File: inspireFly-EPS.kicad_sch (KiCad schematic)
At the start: 182 parts, among them J1 USB4085-GF-A_REVB, J2 Conn_01x02_Pin, J3 FTSH-107-01-L-DV-K-A, Q1 SQJ123ELP-T1_GE3, Q10 SQJA62EP-T1_GE3, Q14 SQJA62EP-T1_GE3, Q15 SQJA62EP-T1_GE3, Q16 SQJA62EP-T1_GE3, Q17 SQJA62EP-T1_GE3, Q3 SQJA62EP-T1_GE3, Q4 SQJA62EP-T1_GE3, Q5 SQJA62EP-T1_GE3, Q6 SQJA62EP-T1_GE3, Q7 SQJA62EP-T1_GE3, Q8 SQJA62EP-T1_GE3, Q9 SQJA62EP-T1_GE3, SW1 SW_Push, SW2 SW_Push, SW3 SW_Push, U1 STM32U575RIT6, U10 BQ25756ERRVR, U13 TPS259472ARPWR, U2 BQ25750RRVR, U3 TCAN332DCNR, U4 MAX77504AAFC+T, U6 INA180A3IDBVT, U7 INA180A3IDBVT, U8 TPS63070RNMR, U9 TPS63070RNMR, Y1 Crystal_GND2

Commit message: Routing Updates
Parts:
- removed C1, C25: 100nF, Capacitor_SMD:C_0402_1005Metric_Pad0.74x0.62mm_HandSolder, symbol Device:C
- removed C26, C51: 10pF, Capacitor_SMD:C_0402_1005Metric_Pad0.74x0.62mm_HandSolder, symbol Device:C
- removed J1: USB4085-GF-A_REVB, inspireFly-EPS-footprints:GCT_USB4085-GF-A_REVB, symbol InspireFly-EPS-sym_lib:USB4085-GF-A_REVB
- removed R18, R19: 10k, Resistor_SMD:R_0402_1005Metric_Pad0.72x0.64mm_HandSolder, symbol Device:R_US
- removed R35, R36: 10K, Resistor_SMD:R_0402_1005Metric_Pad0.72x0.64mm_HandSolder, symbol Device:R_US
- removed SW1, SW2: SW_Push, inspireFly-EPS-footprints:SW_PTS810_SJM_250_SMTR_LFS, symbol Switch:SW_Push
- removed U1: STM32U575RIT6, inspireFly-EPS-footprints:LQFP64-10x10mm_STM, symbol InspireFly-EPS-sym_lib:STM32U575RIT6
- removed Y1: Crystal_GND2, inspireFly-EPS-footprints:XTAL_TSX-3225_16.0000MF18X-AC0, symbol Device:Crystal_GND2
- added C25, C26: 22pF, Capacitor_SMD:C_0402_1005Metric_Pad0.74x0.62mm_HandSolder, symbol Device:C_Small
- added J5: USB4110-GF-A, inspireFly-EPS-footprints:USB4110-GF-A_GCT, symbol inspirefly:USB4110-GF-A
- added R54: 100k, Resistor_SMD:R_0402_1005Metric_Pad0.72x0.64mm_HandSolder, symbol Device:R_US
- added RN1: YC158TJR-072K2L, inspireFly-EPS-footprints:RESCAXE64P320X160X70-10N, symbol inspirefly:YC158TJR-072K2L
- added SW4: SW_TL1015AF160QG, inspireFly-EPS-footprints:SW_TL1015AF160QG, symbol Switch:SW_Push
- added U5: STM32U575CIT6, inspireFly-EPS-footprints:LQFP48-7x7mm_STM, symbol InspireFly-EPS-sym_lib:STM32U575CIT6
- added Y2: XTAL_ABS07-32.768KHZ-T, inspireFly-EPS-footprints:XTAL_ABS07-32.768KHZ-T, symbol Device:Crystal
- C10, C11, C12, C13, C15, C16, C17, C18, C19, C20, C21, C22, C23, C35, C36, C50, D4, D5, L1, Q1, Q10, Q3, Q4, Q5, Q6, Q7, Q8, Q9, R1, R12, R13, R14, R15, R2, R3, R33, R34, R4, R5, R6, R7, R8, R9, TP1, TP2, TP5, U2: now left out of the parts list
- C6: value 10uF -> 1uF
- D1, R20, R21: now not fitted; now left out of the parts list
- JP2: footprint inspirefly:SmallJumper -> Jumper:SolderJumper-2_P1.3mm_Open_TrianglePad1.0x1.5mm
- R37: value 10K -> 10k
- SW3: value SW_Push -> SW_TL1015AF160QG; footprint inspireFly-EPS-footprints:SW_PTS810_SJM_250_SMTR_LFS -> inspireFly-EPS-footprints:SW_TL1015AF160QG
- U10: footprint inspirefly:IC_BQ25756ERRVR -> inspireFly-EPS-footprints:IC_BQ25756ERRVR
- U13: footprint inspirefly:RPW0010A-MFG -> inspireFly-EPS-footprints:RPW0010A-MFG
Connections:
- net +3.3V: now also R37.1, RN1.10, RN1.5, SW4.2, U5.1 (VBAT), U5.24 (VDD), U5.36 (VDD), U5.48 (VDD), U5.9 (VDDA); no longer R37.2
- net ADC1_IN3: now also U5.10 (PA0)
- net ADC1_IN4: now also U5.11 (PA1)
- net EXTERNAL_VOLTAGE: now also D2.1 (K), J2.1 (Pin_1), TP6.1
- net GND: now also C79.2, SW3.2, C25.1, C26.1, J5.15 (Shield), J5.16 (Shield), J5.17 (Shield), J5.18 (Shield), J5.A1-B12 (GND), J5.A12-B1 (GND), R54.1, U5.23 (VSS), U5.35 (VSS), U5.47 (VSS), U5.8 (VSSA); no longer SW3.1
- net I2C2_SCL: now also RN1.4, U5.26 (PB13)
- net I2C2_SDA: now also RN1.3, U5.27 (PB14)
- net JTCK/SWCLK: now also U5.37 (PA14)
- net JTDI: now also U5.38 (PA15)
- net JTMS/SWDIO: now also U5.34 (PA13)
- net NRST: now also R37.2, SW3.1, U5.7 (NRST); no longer R37.1, SW3.2
- net PROTECTED_VOLTAGE: now also C30.1, C37.1, C44.1, U4.12 (SUP), U4.2 (EN), U8.1 (PS/SYNC), U8.12_13 (VIN), U8.14 (EN), U9.1 (PS/SYNC), U9.12_13 (VIN), U9.14 (EN)
- net SWO: now also U5.39 (PB3)
- net USB_CC1: now also J5.A5 (CC1), U5.41 (PB5)
- net USB_CC2: now also J5.B5 (CC2), U5.28 (PB15)
- net USB_V: now also J5.A4-B9 (VBUS), J5.A9-B4 (VBUS)
- net V_BUS_COMBINED: no longer D2.1 (K), J2.1 (Pin_1), TP6.1
- net V_PROTECTED: no longer C30.1, C37.1, C44.1, U4.12 (SUP), U4.2 (EN), U8.1 (PS/SYNC), U8.12_13 (VIN), U8.14 (EN), U9.1 (PS/SYNC), U9.12_13 (VIN), U9.14 (EN)
- net DEBUG_LPUART_TX: now reaches J3.13
- net DEBUG_LPUART_TX: now also U5.12 (PA2)
- net DEBUG_LPUART_RX: now reaches J3.14
- net DEBUG_LPUART_RX: now also U5.13 (PA3)
- net at C2.1: now also U5.22 (VCAP)
- new net: C25.2, U5.3 (PC14-OSC32_IN), Y2.1
- new net: C26.2, U5.4 (PC15-OSC32_OUT), Y2.2
- new net BOOT0: R54.2, SW4.1, U5.44 (PH3-BOOT0)
- new net CAN_RXD: U5.32 (PA11)
- new net CAN_TXD: U5.33 (PA12)
- new net I2C1_SCL: RN1.2, U5.45 (PB8)
- new net I2C1_SDA: RN1.1, U5.46 (PB9)
- new net I2C3_SCL: RN1.8, U5.17 (PA7)
- new net I2C3_SDA: RN1.9, U5.40 (PB4)
- new net I2C4_SCL: RN1.6, U5.21 (PB10)
- new net I2C4_SDA: RN1.7, U5.43 (PB7)
- no-connect marks 19 -> 21
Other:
- note removed: "NRST Circuit"

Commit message: Schematic Updates
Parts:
- added C80: 22uF, Capacitor_SMD:C_0805_2012Metric_Pad1.18x1.45mm_HandSolder, symbol Device:C
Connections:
- net EXTERNAL_VOLTAGE: now also C80.1
- net GND: now also C80.2
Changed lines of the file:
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@@
 	)
 	(junction
+		(at 261.62 193.04)
+		(diameter 0)
+		(color 0 0 0 0)
+	)
+	(junction
 		(at 265.43 566.42)
 		(diameter 0)
@@
 	)
 	(symbol
+		(lib_id "Device:C")
+		(at 261.62 189.23 180)
+		(unit 1)
+		(body_style 1)
+		(exclude_from_sim no)
+		(in_bom yes)
+		(on_board yes)
+		(in_pos_files yes)
+		(dnp no)
+		(fields_autoplaced yes)
+		(property "Reference" "C80"
+			(at 257.81 190.5001 0)
+			(show_name no)
+			(do_not_autoplace no)
+			(effects
+				(font
+					(size 1.27 1.27)
+				)
+				(justify left)
+			)
+		)
+		(property "Value" "22uF"
+			(at 257.81 187.9601 0)
+			(show_name no)
+			(do_not_autoplace no)
+			(effects
+				(font
+					(size 1.27 1.27)
+				)
+				(justify left)
+			)
+		)
+		(property "Footprint" "Capacitor_SMD:C_0805_2012Metric_Pad1.18x1.45mm_HandSolder"
+			(at 260.6548 185.42 0)
+			(hide yes)
+			(show_name no)
+			(do_not_autoplace no)
+			(effects
+				(font
+					(size 1.27 1.27)
+				)
+			)
+		)
+		(property "Datasheet" ""
+			(at 261.62 189.23 0)
+			(hide yes)
+			(show_name no)
+			(do_not_autoplace no)
+			(effects
+				(font
+					(size 1.27 1.27)
+				)
+			)
+		)
+		(property "Description" "Unpolarized capacitor"
+			(at 261.62 189.23 0)
+			(hide yes)
+			(show_name no)
+			(do_not_autoplace no)
+			(effects
+				(font
+					(size 1.27 1.27)
+				)
+			)
+		)
+		(pin "2"
+		)
+		(pin "1"
+		)
+		(instances
+			(project "inspireFly-EPS"
+				(path "/85d7bd69-2813-405d-9eae-82e9bb551a95"
+					(reference "C80")
+					(unit 1)
+				)
+			)
+		)
+	)
+	(symbol
 		(lib_id "power:+3.3V")
 		(at 231.14 83.82 0)
@@
 					(unit 1)
 				)
+			)
+		)
+	)
+	(symbol
+		(lib_id "power:GND")
+		(at 261.62 185.42 180)
+		(unit 1)
+		(body_style 1)
+		(exclude_from_sim no)
+		(in_bom yes)
+		(on_board yes)
+		(in_pos_files yes)
+		(dnp no)
+		(property "Reference" "#PWR0125"
+			(at 261.62 179.07 0)
+			(hide yes)
+			(show_name no)
+			(do_not_autoplace no)
+			(effects
+				(font
+					(size 1.27 1.27)
+				)
+			)
+		)
+		(property "Value" "GND"
+			(at 261.366 181.61 0)
+			(show_name no)
+			(do_not_autoplace no)
+			(effects
+				(font
+					(size 1.27 1.27)
+				)
+			)
+		)
+		(property "Footprint" ""
+			(at 261.62 185.42 0)
+			(hide yes)
+			(show_name no)
+			(do_not_autoplace no)
+			(effects
+				(font
+					(size 1.27 1.27)
+				)
+			)
+		)
+		(property "Datasheet" ""
+			(at 261.62 185.42 0)
+			(hide yes)
+			(show_name no)
+			(do_not_autoplace no)
+			(effects
+				(font
+					(size 1.27 1.27)
+				)
+			)
+		)
+		(property "Description" "Power symbol creates a global label with name \"GND\" , ground"
+			(at 261.62 185.42 0)
+			(hide yes)
+			(show_name no)
+			(do_not_autoplace no)
+			(effects
+				(font
+					(size 1.27 1.27)
+				)
+			)
+		)
+		(pin "1"
+		)
+		(instances
+			(project "inspireFly-EPS"
+				(path "/85d7bd69-2813-405d-9eae-82e9bb551a95"
+					(reference "#PWR0125")
+					(unit 1)
+				)

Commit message: 3.3V routing changes
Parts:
- removed C34, C41: 22uF, Capacitor_SMD:C_0805_2012Metric_Pad1.18x1.45mm_HandSolder, symbol Device:C
- added J4: Conn_01x02_Pin, Connector_PinSocket_2.54mm:PinSocket_1x02_P2.54mm_Vertical, symbol Connector:Conn_01x02_Pin
- C30, C37, C38, C44, C45: footprint Capacitor_SMD:C_0805_2012Metric_Pad1.18x1.45mm_HandSolder -> Capacitor_SMD:C_0402_1005Metric_Pad0.74x0.62mm_HandSolder
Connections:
- net CAN_H: now also J4.1 (Pin_1)
- net CAN_L: now also J4.2 (Pin_2)
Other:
- moved on the sheet: C31, C42, C43

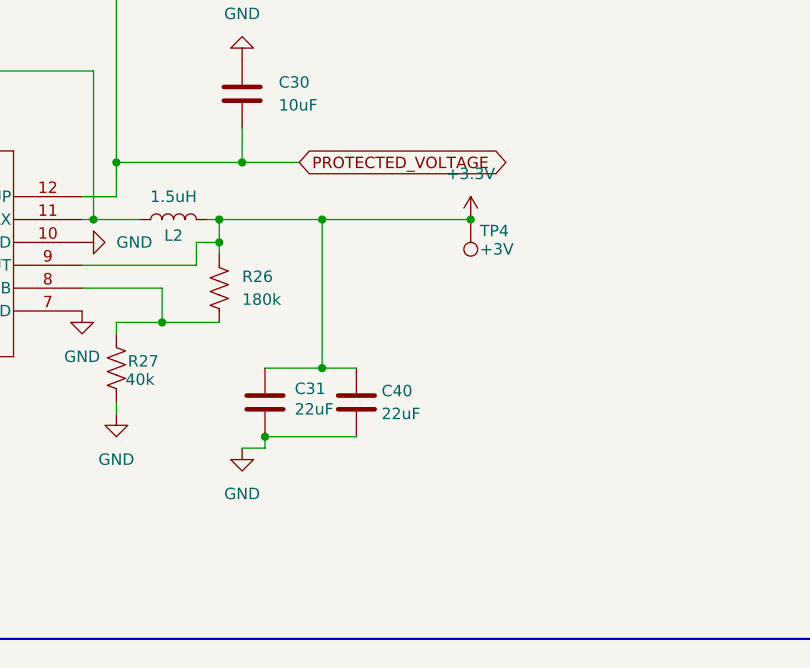
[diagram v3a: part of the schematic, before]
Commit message: Pushing routing changes, finailize vreg locations
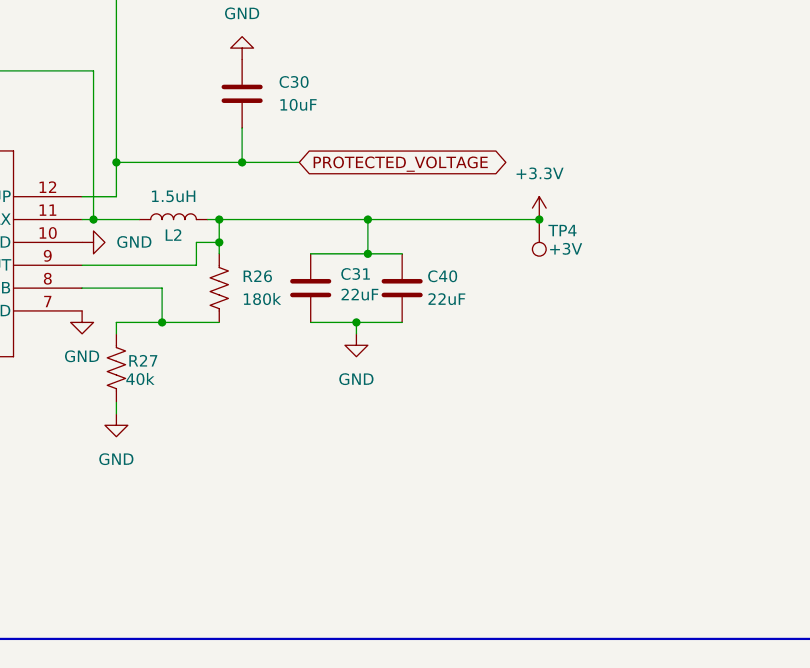
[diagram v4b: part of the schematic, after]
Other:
- moved on the sheet: C31, C40, TP4
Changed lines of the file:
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@@
 	)
 	(junction
-		(at 102.87 588.01)
+		(at 429.26 213.36)
 		(diameter 0)
 		(color 0 0 0 0)
 	)
 	(junction
-		(at 194.31 86.36)
+		(at 102.87 588.01)
 		(diameter 0)
 		(color 0 0 0 0)
 	)
 	(junction
-		(at 134.62 566.42)
+		(at 194.31 86.36)
 		(diameter 0)
 		(color 0 0 0 0)
 	)
 	(junction
-		(at 218.44 566.42)
+		(at 134.62 566.42)
 		(diameter 0)
 		(color 0 0 0 0)
 	)
 	(junction
-		(at 421.64 213.36)
+		(at 218.44 566.42)
 		(diameter 0)
 		(color 0 0 0 0)
@@
 	)
 	(junction
-		(at 405.13 213.36)
+		(at 410.21 213.36)
+		(diameter 0)
+		(color 0 0 0 0)
+	)
+	(junction
+		(at 408.94 224.79)
 		(diameter 0)
 		(color 0 0 0 0)
@@
 	)
 	(junction
-		(at 398.78 237.49)
-		(diameter 0)
-		(color 0 0 0 0)
-	)
-	(junction
 		(at 187.96 222.25)
 		(diameter 0)
@@
 	)
 	(junction
-		(at 405.13 229.87)
+		(at 410.21 217.17)
 		(diameter 0)
 		(color 0 0 0 0)
@@
 	(wire
 		(pts
-			(xy 398.78 238.76) (xy 396.24 238.76)
+			(xy 408.94 224.79) (xy 408.94 226.06)
 		)
 		(stroke
@@
 	(wire
 		(pts
-			(xy 398.78 237.49) (xy 408.94 237.49)
+			(xy 403.86 224.79) (xy 408.94 224.79)
 		)
 		(stroke
@@
 	(wire
 		(pts
-			(xy 405.13 213.36) (xy 405.13 229.87)
+			(xy 410.21 213.36) (xy 410.21 217.17)
 		)
 		(stroke
@@
 	(wire
 		(pts
-			(xy 398.78 238.76) (xy 398.78 237.49)
+			(xy 295.91 370.84) (xy 295.91 372.11)
 		)
 		(stroke
@@
 	(wire
 		(pts
-			(xy 295.91 370.84) (xy 295.91 372.11)
+			(xy 477.52 284.48) (xy 477.52 281.94)
 		)
 		(stroke
@@
 	(wire
 		(pts
-			(xy 477.52 284.48) (xy 477.52 281.94)
+			(xy 74.93 368.3) (xy 74.93 359.41)
 		)
 		(stroke
@@
 	(wire
 		(pts
-			(xy 74.93 368.3) (xy 74.93 359.41)
+			(xy 105.41 494.03) (xy 128.27 494.03)
 		)
 		(stroke
@@
 	(wire
 		(pts
-			(xy 105.41 494.03) (xy 128.27 494.03)
+			(xy 321.31 226.06) (xy 321.31 220.98)
 		)
 		(stroke
@@
 	(wire
 		(pts
-			(xy 321.31 226.06) (xy 321.31 220.98)
+			(xy 337.82 60.96) (xy 355.6 60.96)
 		)
 		(stroke
@@
 	(wire
 		(pts
-			(xy 337.82 60.96) (xy 355.6 60.96)
+			(xy 408.94 224.79) (xy 414.02 224.79)
 		)
 		(stroke
@@
 	(wire
 		(pts
-			(xy 393.7 213.36) (xy 405.13 213.36)
+			(xy 393.7 213.36) (xy 410.21 213.36)
 		)
 		(stroke
@@
 	(wire
 		(pts
-			(xy 405.13 213.36) (xy 421.64 213.36)
-		)
-		(stroke
-			(width 0)
-			(type default)
-		)
-	)
-	(wire
-		(pts
 			(xy 220.98 382.27) (xy 306.07 382.27)
 		)
@@
 	(wire
 		(pts
+			(xy 410.21 213.36) (xy 429.26 213.36)
+		)
+		(stroke
+			(width 0)
+			(type default)
+		)
+	)
+	(wire
+		(pts
 			(xy 260.35 342.9) (xy 271.78 342.9)
 		)
@@
 	(wire
 		(pts
-			(xy 398.78 229.87) (xy 405.13 229.87)
+			(xy 403.86 217.17) (xy 410.21 217.17)
 		)
 		(stroke
@@
 	(wire
 		(pts
-			(xy 405.13 229.87) (xy 408.94 229.87)
+			(xy 410.21 217.17) (xy 414.02 217.17)
 		)
 		(stroke
@@
 	(symbol
 		(lib_id "power:+3.3V")
-		(at 421.64 213.36 0)
+		(at 429.26 213.36 0)
 		(unit 1)
 		(body_style 1)
@@
 		(fields_autoplaced yes)
 		(property "Reference" "#PWR037"
-			(at 421.64 217.17 0)
+			(at 429.26 217.17 0)
 			(hide yes)
 			(show_name no)
@@
 		)
 		(property "Value" "+3.3V"
-			(at 421.64 208.28 0)
+			(at 429.26 208.28 0)
 			(show_name no)
 			(do_not_autoplace no)
@@
 		)
 		(property "Footprint" ""
-			(at 421.64 213.36 0)
+			(at 429.26 213.36 0)
 			(hide yes)
 			(show_name no)
@@
 		)
 		(property "Datasheet" ""
-			(at 421.64 213.36 0)
+			(at 429.26 213.36 0)
 			(hide yes)
 			(show_name no)
@@
 		)
 		(property "Description" "Power symbol creates a global label with name \"+3.3V\""
-			(at 421.64 213.36 0)
+			(at 429.26 213.36 0)
 			(hide yes)
 			(show_name no)
@@
 	(symbol
 		(lib_id "Device:C")
-		(at 408.94 233.68 180)
+		(at 414.02 220.98 180)
 		(unit 1)
 		(body_style 1)
@@
 		(dnp no)
 		(property "Reference" "C40"
-			(at 411.734 232.41 0)
+			(at 416.814 219.71 0)
 			(show_name no)
 			(do_not_autoplace no)
@@
 		)
 		(property "Value" "22uF"
-			(at 411.734 234.95 0)
+			(at 416.814 222.25 0)
 			(show_name no)
 			(do_not_autoplace no)
@@
 		)
 		(property "Footprint" "Capacitor_SMD:C_0805_2012Metric_Pad1.18x1.45mm_HandSolder"
-			(at 407.9748 229.87 0)
+			(at 413.0548 217.17 0)
 			(hide yes)
 			(show_name no)
@@
 		)
 		(property "Datasheet" ""
-			(at 408.94 233.68 0)
+			(at 414.02 220.98 0)
 			(hide yes)
 			(show_name no)
@@
 		)
 		(property "Description" "Unpolarized capacitor"
-			(at 408.94 233.68 0)
+			(at 414.02 220.98 0)
 			(hide yes)
 			(show_name no)
@@
 	(symbol
 		(lib_id "Connector:TestPoint")
-		(at 421.64 213.36 180)
+		(at 429.26 213.36 180)
 		(unit 1)
 		(body_style 1)
@@
 		(dnp no)
 		(property "Reference" "TP4"
-			(at 422.656 214.63 0)
+			(at 430.276 214.63 0)
 			(show_name no)
 			(do_not_autoplace no)
@@
 		)
 		(property "Value" "+3V"
-			(at 422.656 216.662 0)
+			(at 430.276 216.662 0)
 			(show_name no)
 			(do_not_autoplace no)
@@
 		)
 		(property "Footprint" "TestPoint:TestPoint_Pad_D1.5mm"
-			(at 416.56 213.36 0)
+			(at 424.18 213.36 0)
 			(hide yes)
 			(show_name no)
@@
 		)
 		(property "Datasheet" ""
-			(at 416.56 213.36 0)
+			(at 424.18 213.36 0)
 			(hide yes)
 			(show_name no)
@@
 		)
 		(property "Description" "test point"
-			(at 421.64 213.36 0)
+			(at 429.26 213.36 0)
 			(hide yes)
 			(show_name no)
@@
 	(symbol
 		(lib_id "Device:C")
-		(at 398.78 233.68 180)
+		(at 403.86 220.98 180)
 		(unit 1)
 		(body_style 1)
@@
 		(dnp no)
 		(property "Reference" "C31"
-			(at 402.082 232.156 0)
+			(at 407.162 219.456 0)
 			(show_name no)
 			(do_not_autoplace no)
@@
 		)
 		(property "Value" "22uF"
-			(at 402.082 234.442 0)
+			(at 407.162 221.742 0)
 			(show_name no)
 			(do_not_autoplace no)
@@
 		)
 		(property "Footprint" "Capacitor_SMD:C_0805_2012Metric_Pad1.18x1.45mm_HandSolder"
-			(at 397.8148 229.87 0)
+			(at 402.8948 217.17 0)
 			(hide yes)
 			(show_name no)
@@
 		)
 		(property "Datasheet" ""
-			(at 398.78 233.68 0)
+			(at 403.86 220.98 0)
 			(hide yes)
 			(show_name no)
@@
 		)
 		(property "Description" "Unpolarized capacitor"
-			(at 398.78 233.68 0)
+			(at 403.86 220.98 0)
 			(hide yes)
 			(show_name no)
@@
 	(symbol
 		(lib_id "power:GND")
-		(at 396.24 238.76 0)
+		(at 408.94 226.06 0)
 		(unit 1)
 		(body_style 1)
@@
 		(fields_autoplaced yes)
 		(property "Reference" "#PWR047"
-			(at 396.24 245.11 0)
+			(at 408.94 232.41 0)
 			(hide yes)
 			(show_name no)
@@
 		)
 		(property "Value" "GND"
-			(at 396.24 243.84 0)
+			(at 408.94 231.14 0)
 			(show_name no)
 			(do_not_autoplace no)
@@
 		)
 		(property "Footprint" ""
-			(at 396.24 238.76 0)
+			(at 408.94 226.06 0)
 			(hide yes)
 			(show_name no)
@@
 		)
 		(property "Datasheet" ""
-			(at 396.24 238.76 0)
+			(at 408.94 226.06 0)
 			(hide yes)
 			(show_name no)
@@
 		)
 		(property "Description" "Power symbol creates a global label with name \"GND\" , ground"
-			(at 396.24 238.76 0)
+			(at 408.94 226.06 0)
 			(hide yes)
 			(show_name no)

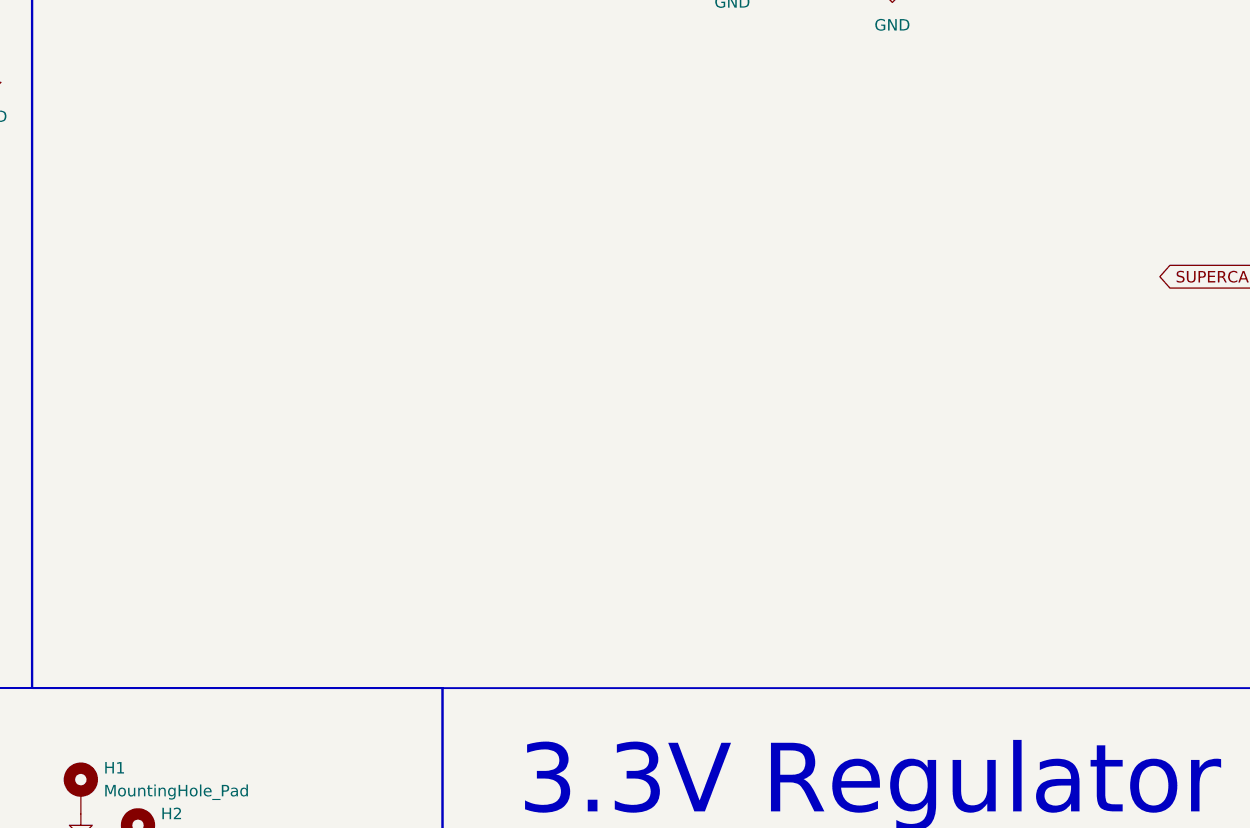
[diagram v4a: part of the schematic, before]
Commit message: Added linear charger to schematic
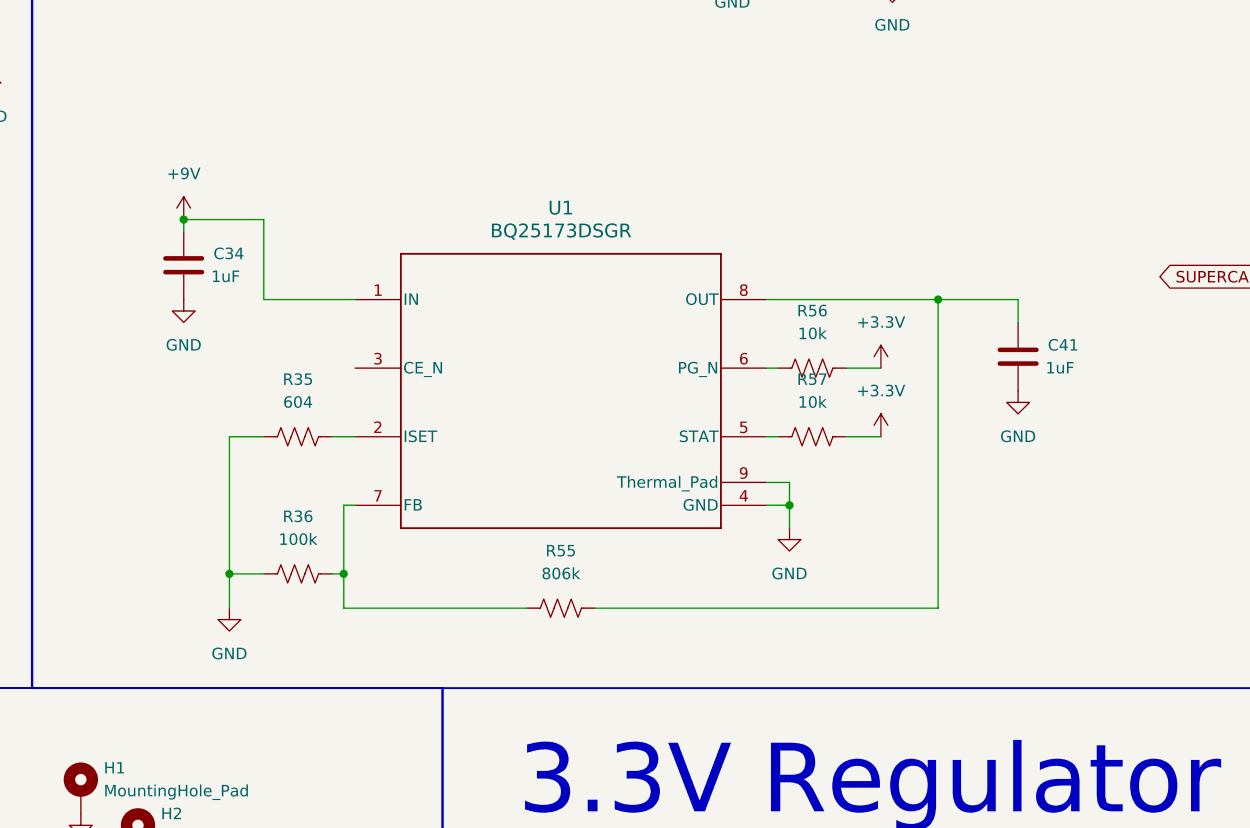
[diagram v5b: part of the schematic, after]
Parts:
- added C34, C41: 1uF, Capacitor_SMD:C_0402_1005Metric_Pad0.74x0.62mm_HandSolder, symbol Device:C
- added R35: 604, Resistor_SMD:R_0402_1005Metric_Pad0.72x0.64mm_HandSolder, symbol Device:R_US
- added R36: 100k, Resistor_SMD:R_0402_1005Metric_Pad0.72x0.64mm_HandSolder, symbol Device:R_US
- added R55: 806k, Resistor_SMD:R_0402_1005Metric_Pad0.72x0.64mm_HandSolder, symbol Device:R_US
- added R56, R57: 10k, Resistor_SMD:R_0402_1005Metric_Pad0.72x0.64mm_HandSolder, symbol Device:R_US
- added U1: BQ25173DSGR, inspireFly-EPS-footprints:DSG0008A-IPC_B, symbol InspireFly-EPS-sym_lib:BQ25173DSGR
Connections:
- net +3.3V: now also R56.1, R57.1
- net +9V: now also C34.1, U1.1 (IN)
- net GND: now also C34.2, C41.2, R35.2, R36.2, U1.4 (GND), U1.9 (Thermal_Pad)
- new net: R36.1, R55.2, U1.7 (FB)
- new net: R35.1, U1.2 (ISET)
- new net: R57.2, U1.5 (STAT)
- new net: R56.2, U1.6 (PG_N)
- new net: C41.1, R55.1, U1.8 (OUT)
